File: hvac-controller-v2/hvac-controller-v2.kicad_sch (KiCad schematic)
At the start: 48 parts, among them J1 VAC IN, J2 Conn_01x06, J3 UART, U1 LY68L6400SLIT, U2 ESP32-PICO-D4, U4 TPS5430DDA, U5 TPS5430DDA, U6 LM324DT

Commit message: Laid out board, sans boot jumper
Trying to figure out if I can hook this up to serial somehow.
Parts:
- removed AE1: Antenna_Shield, kelvie:Texas_SWRA117D_2.4GHz_Right, symbol Device:Antenna_Shield
- removed C7: 0.1uF, Capacitor_SMD:C_0402_1005Metric, symbol Device:C_Small
- removed R9: 33, Resistor_SMD:R_0402_1005Metric, symbol Device:R_Small
- removed U1: LY68L6400SLIT, Package_SO:SOIC-8_3.9x4.9mm_P1.27mm, symbol kelvie:LY68L6400
- removed U2: ESP32-PICO-D4, Package_DFN_QFN:QFN-48-1EP_7x7mm_P0.5mm_EP5.3x5.3mm, symbol RF_Module:ESP32-PICO-D4
- added C3, C4: 1uF/5V, Capacitor_SMD:C_0402_1005Metric, symbol Device:C_Polarized_Small
- added R2, R3: 1.1k, Resistor_SMD:R_0402_1005Metric, symbol Device:R_Small
- added U1: ESP32-C3-MINI-1, Espressif:ESP32-C3-MINI-1, symbol Espressif:ESP32-C3-MINI-1
- C1: renamed from C10; value 0.01uF -> 0.01uF/16V
- C11: renamed from C3; value 0.1uF -> 0.1uF/16V
- C12: renamed from C11; value 0.1uF -> 0.1uF/16V
- C9: value 470uF/6.3V -> 100uF/16V
- renumbered C8 to C10, C4 to C2, C1 to C5, C2 to C6, C5 to C7, C6 to C8, D3 to D2, D2 to D3, H6 to H3, H7 to H4, H3 to H6, H4 to H7, L2 to L1, L1 to L2, R11 to R1, R3 to R10, R14 to R11, R4 to R12, R15 to R13, R7 to R14, R8 to R15, R10 to R17, R1 to R4, R12 to R5, R2 to R6, R13 to R7, R5 to R8, R6 to R9, U6 to U2, U4 to U3, U5 to U4
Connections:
- net ADC1: now also U1.12 (GPIO0/ADC1_CH0/XTAL_32K_P)
- net ADC2: now also U1.13 (GPIO1/ADC1_CH1/XTAL_32K_N)
- net BOOT: now also U1.23 (GPIO9)
- net CHIP_PU: now also U1.8 (EN/CHIP_PU)
- net GND: now also R14.1, C3.2, C4.2, U1.1 (GND), U1.11 (GND), U1.14 (GND), U1.2 (GND), U1.36 (GND)
- net UART_RX: now also U1.30 (GPIO20/U0RXD)
- net UART_TX: now also U1.31 (GPIO21/U0TXD)
- net 24VAC+ renamed -24VA
- net -24VA: now also D1.1; no longer D1.2
- net 24VAC- renamed +24VA
- net +24VA: now also D1.2; no longer D1.1
- net DAC1: no longer names the net of U2.3 (+)
- net DAC1: now also C3.1, R2.1
- net DAC2: no longer names the net of U2.5 (+)
- net DAC2: now also C4.1, R3.1
- net VCC12 renamed +12V
- net VCC33 renamed +3V3
- net +3V3: now also U1.3 (3V3)
- new net PWM1: R2.2, U1.5 (GPIO2/ADC1_CH2)
- new net PWM2: R3.2, U1.6 (GPIO3/ADC1_CH3)
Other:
- note added: "0-3V3 PWM -> lowpass -> 0-10V for control"
- note added: "GPIO shifters"
- note added: "TODO: use different op-amp (MCP6H04)"
- note removed: "0-3V3 -> 0-10V for control"
- note removed: "GPIO shifters (500 uA each)"
- note removed: "PSRAM (400 uA)"
- note removed: "alternatively use a 3216 ANT3216LL00R2400A"
- moved on the sheet: C1, C2, D1, J1, J2, J3, JP1, R1, U2E

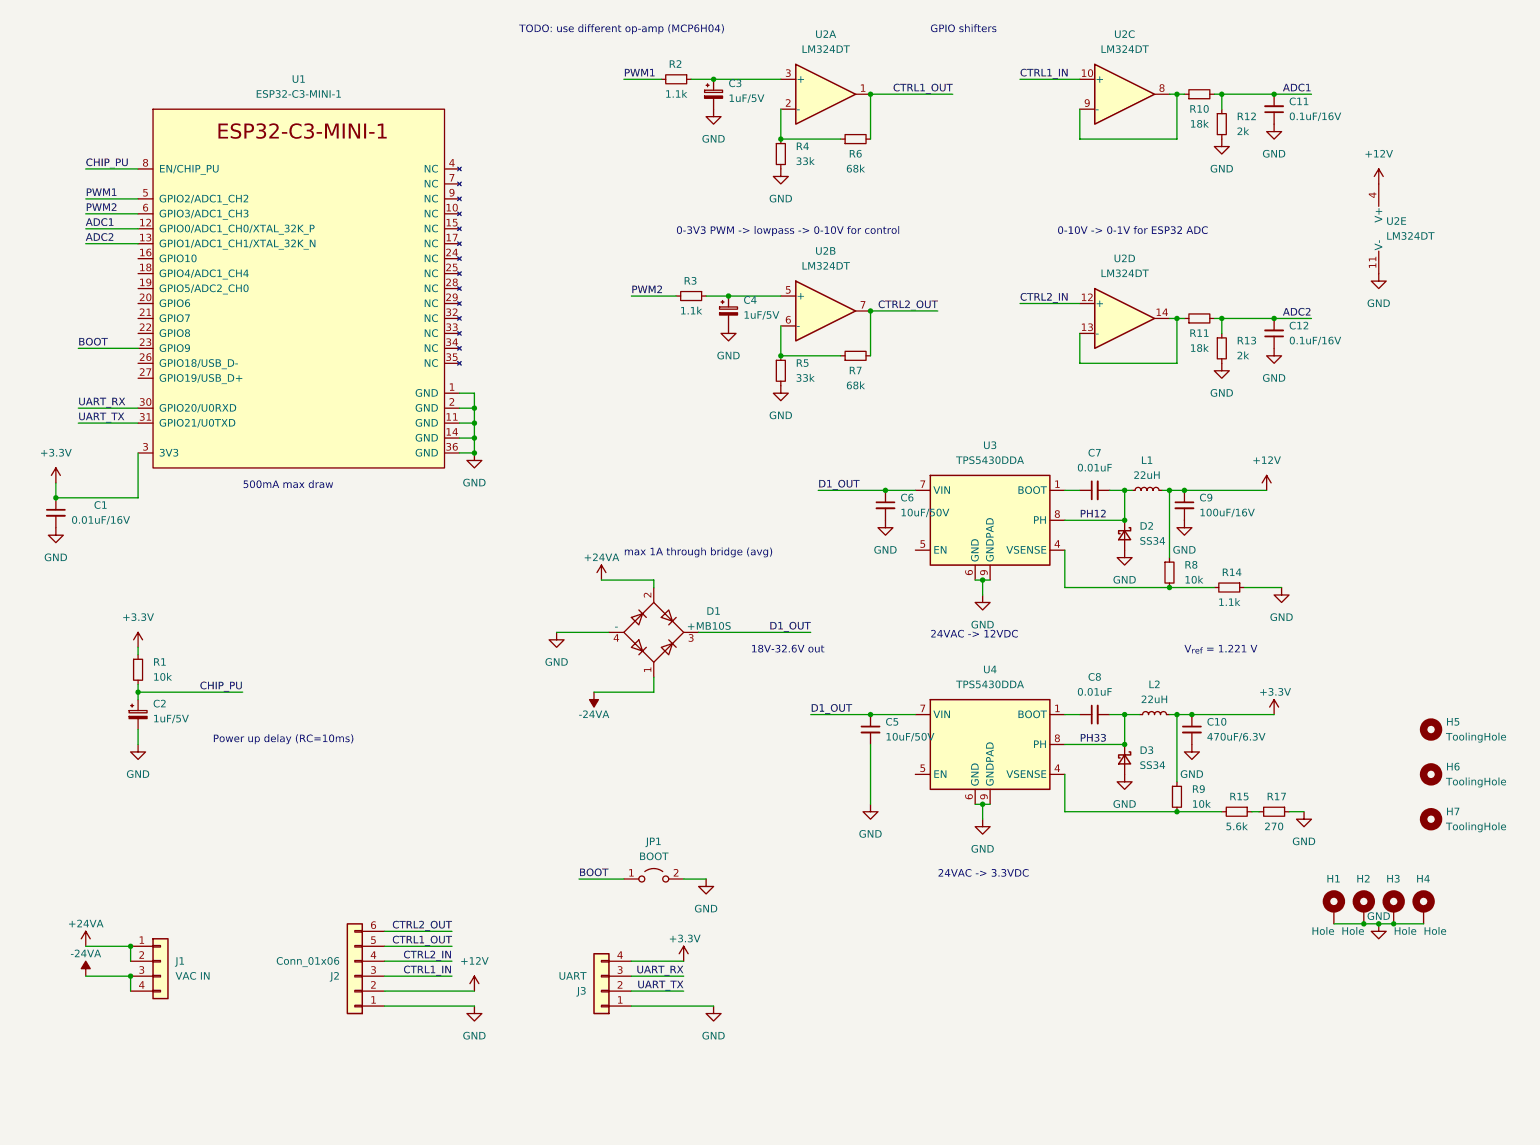
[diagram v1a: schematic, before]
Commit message: Re-layout schematic and PCB
I wanted the antenna on top (long edge).
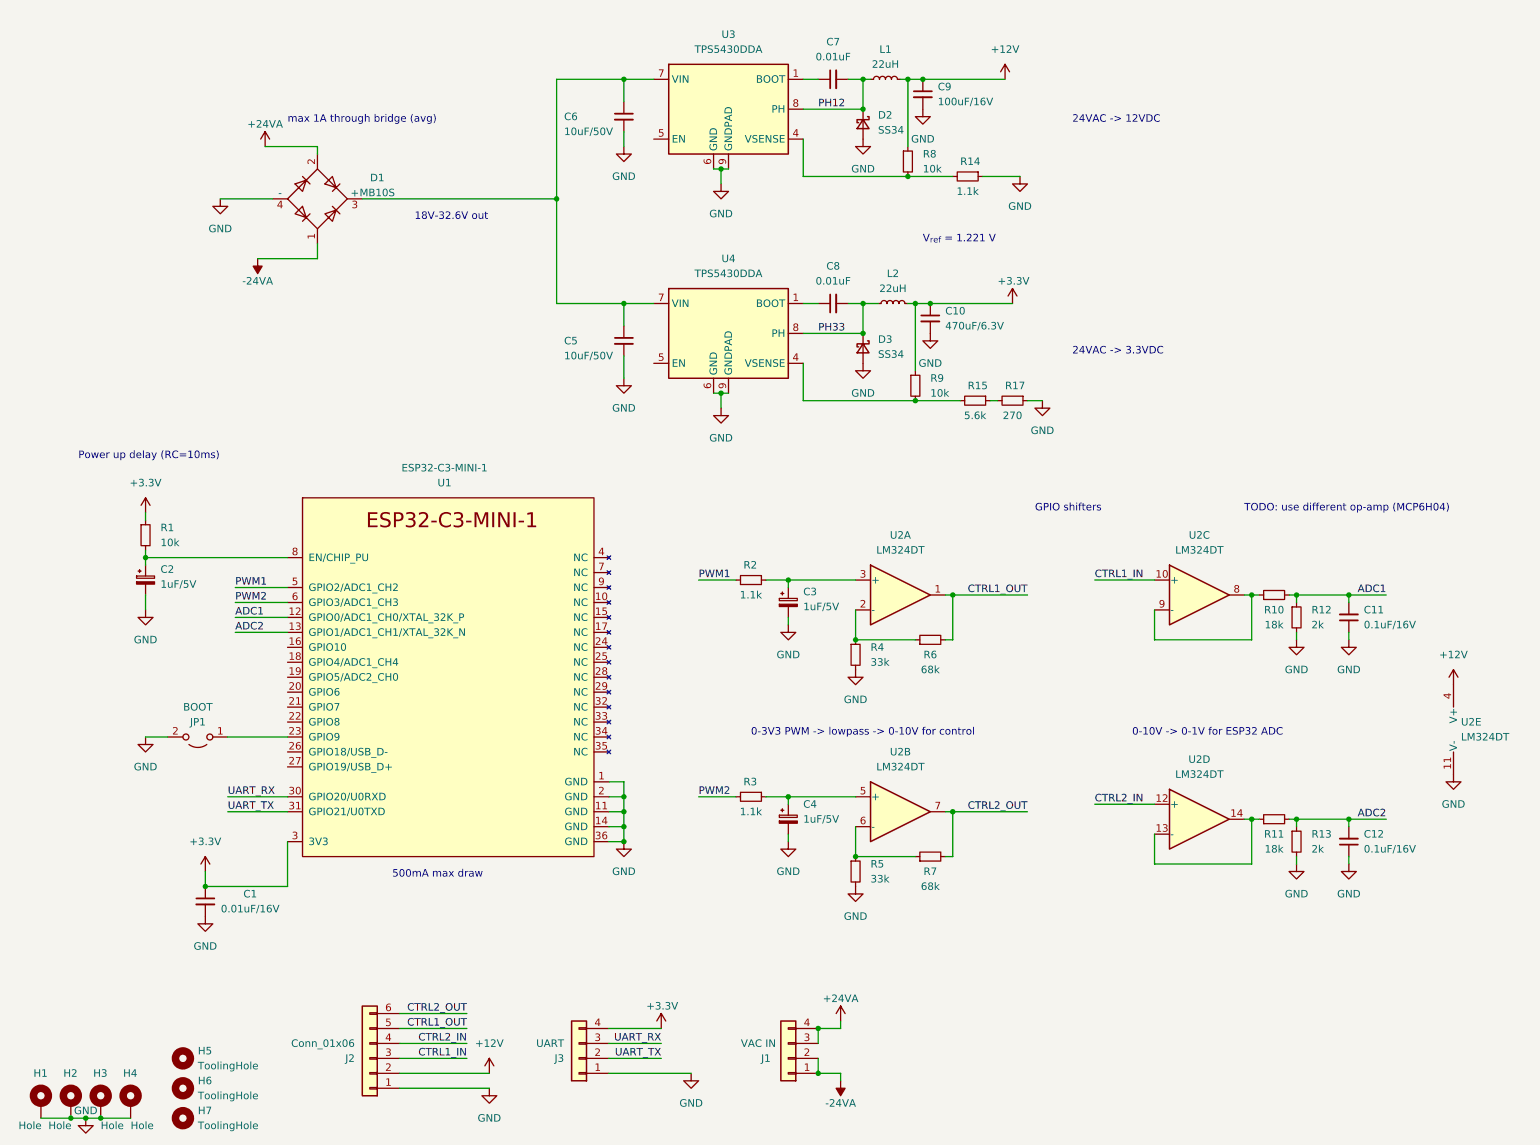
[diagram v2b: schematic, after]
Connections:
- net +24VA: now also J1.3 (Pin_3), J1.4 (Pin_4); no longer J1.1 (Pin_1), J1.2 (Pin_2)
- net -24VA: now also J1.1 (Pin_1), J1.2 (Pin_2); no longer J1.3 (Pin_3), J1.4 (Pin_4)
- net BOOT: no longer names the net of JP1.1 (A), U1.23 (GPIO9)
- net CHIP_PU: no longer names the net of C2.1, R1.2, U1.8 (EN/CHIP_PU)
- net D1_OUT: no longer names the net of C5.1, C6.1, D1.3 (+), U3.7 (VIN), U4.7 (VIN)
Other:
- moved on the sheet: C1, C10, C11, C12, C2, C3, C4, C5, C6, C7, C8, C9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
